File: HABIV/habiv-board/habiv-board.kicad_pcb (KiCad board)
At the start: 4 copper layers, 113 parts, among them IC1 RTC_PCF8523T, J10 Conn_01x08_Male, J2 Conn_ARM_JTAG_SWD_20, J3 Conn_01x02_Male, J4 Conn_01x16_Male, J5 Conn_01x02_Male, J6 Conn_01x16_Male, J7 Conn_01x16_Male, J8 Conn_01x08_Male, J9 Conn_01x02_Male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

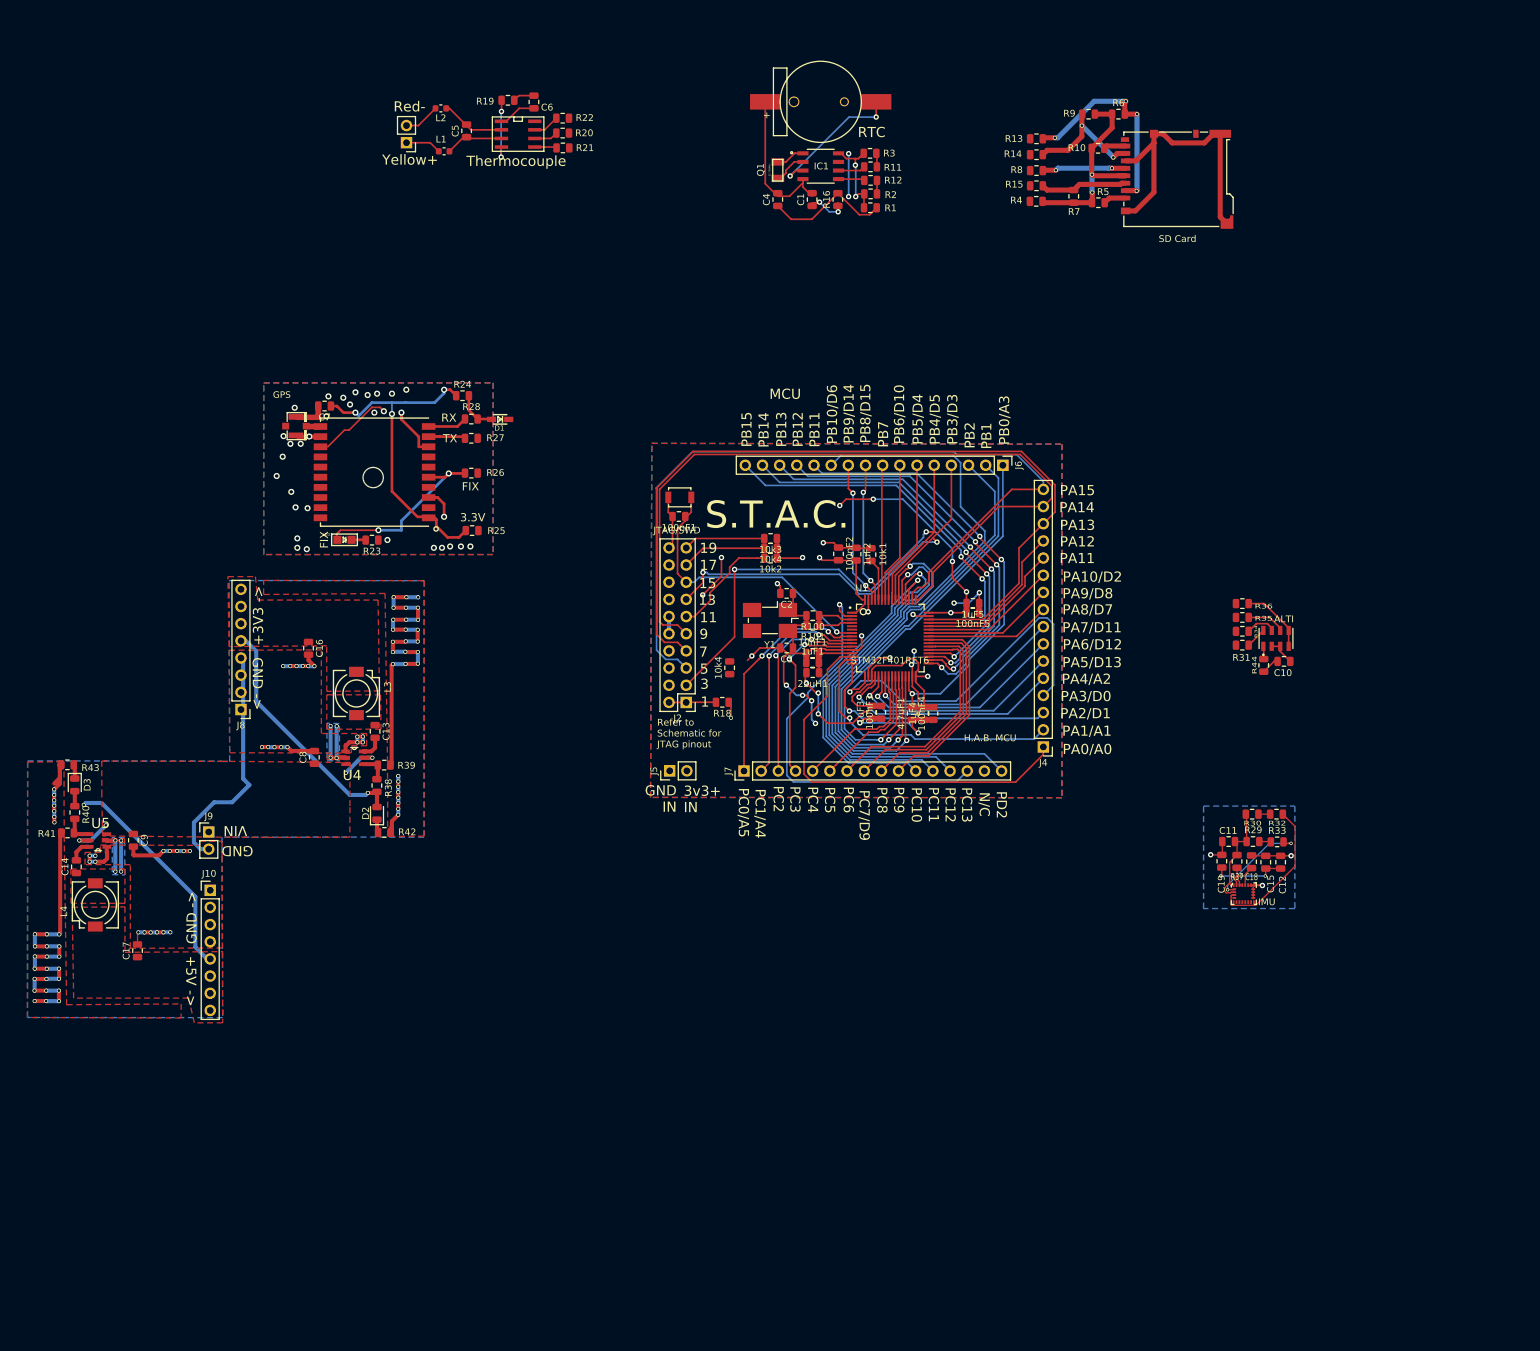
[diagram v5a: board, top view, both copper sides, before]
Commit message: begin to route together final nets
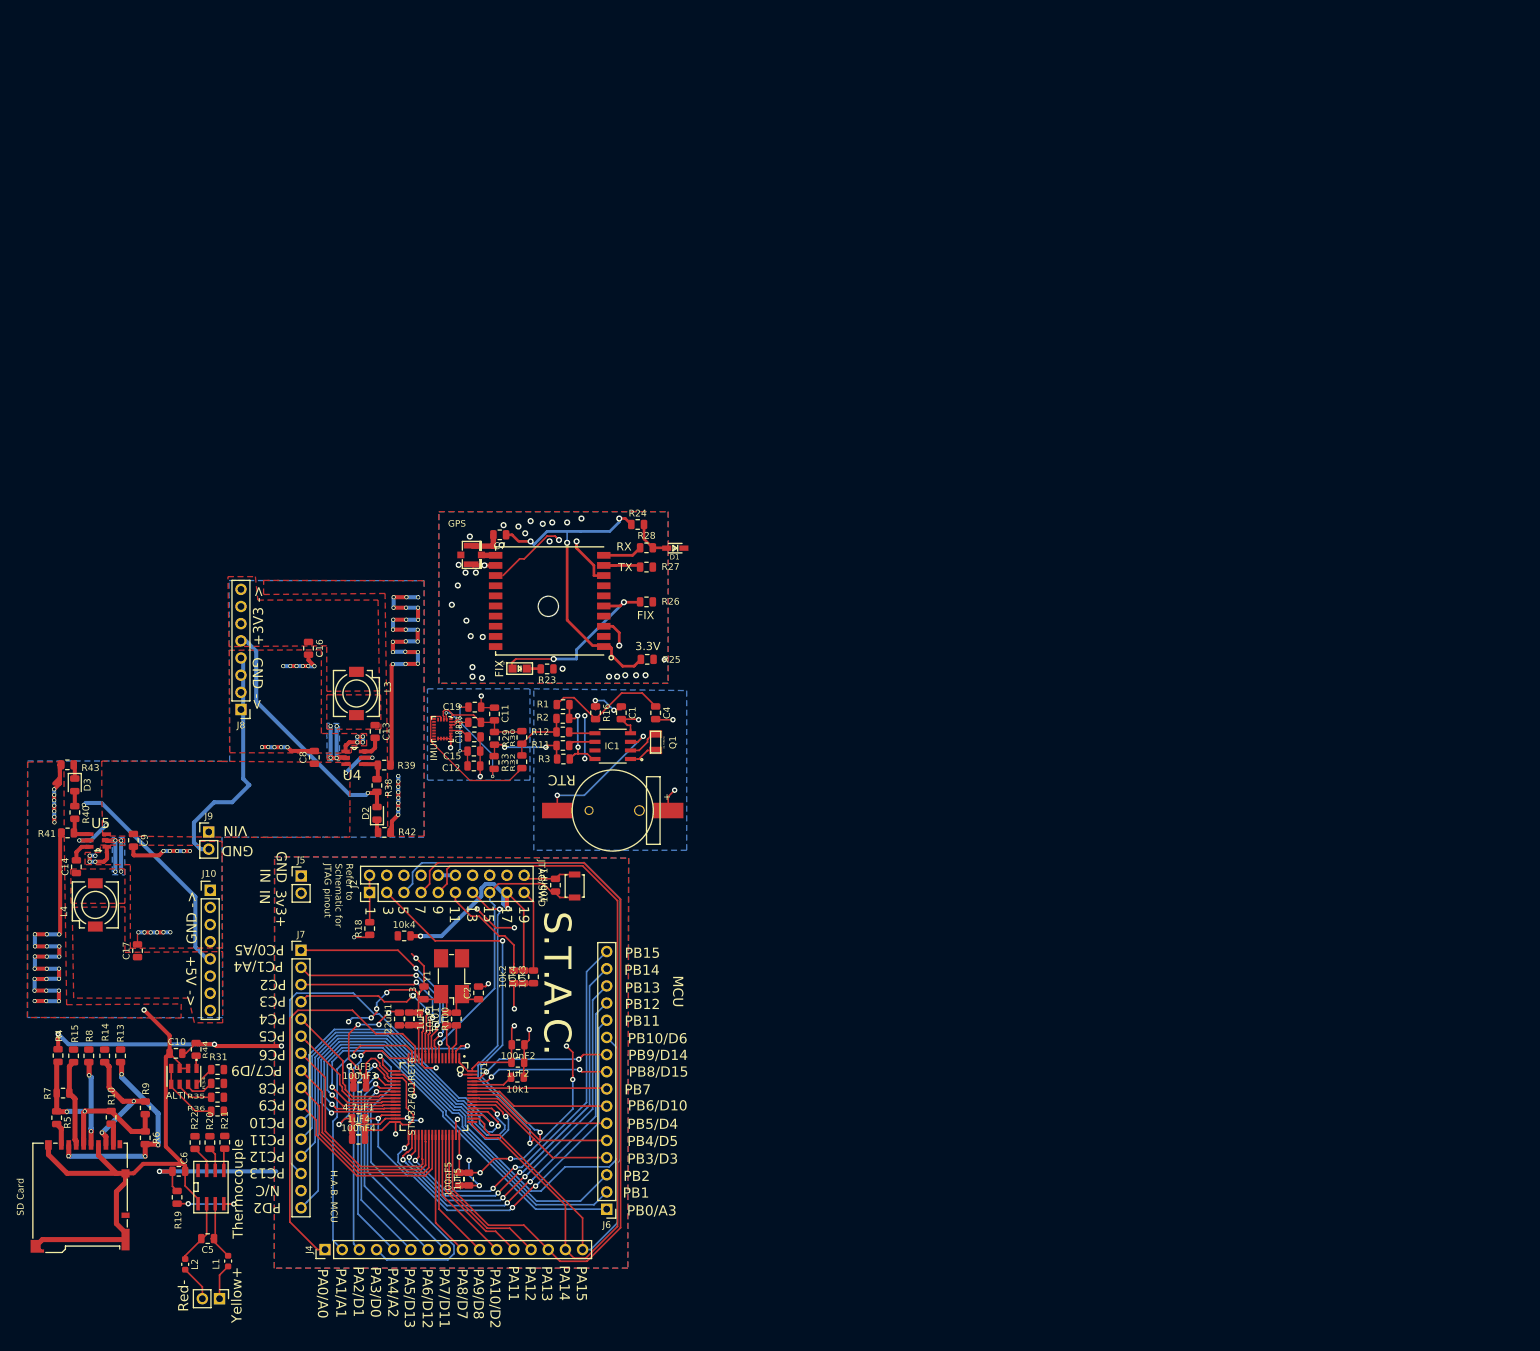
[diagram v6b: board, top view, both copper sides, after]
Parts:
- moved SD Card 221.3 mm to (24.1, 183.8), turned to 0 degrees
- moved R6 208.9 mm to (33.7, 175.1), turned to 270 degrees
- moved R5 205.1 mm to (20.6, 172.1), turned to 270 degrees
- moved R10 204.6 mm to (28.7, 172.1), turned to 270 degrees
- moved R9 202.7 mm to (33.7, 170.7), turned to 90 degrees
- moved R7 199.9 mm to (21.5, 168.5), turned to 180 degrees
- moved R4 192.1 mm to (20.8, 163.0), turned to 270 degrees
- moved R15 192.0 mm to (23.1, 163.0), turned to 270 degrees
- moved R8 191.8 mm to (25.4, 163.0), turned to 90 degrees
- moved R14 191.7 mm to (27.7, 163.0), turned to 90 degrees
- moved R13 191.7 mm to (30.1, 163.0), turned to 270 degrees
- moved L2 175.1 mm to (39.6, 193.8), turned to 270 degrees
- moved U7 174.1 mm to (39.4, 166.0), turned to 270 degrees
- moved C10 173.8 mm to (38.2, 162.6), turned to 180 degrees
- moved J3 173.2 mm to (44.7, 198.9), turned to 270 degrees
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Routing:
- net +3V3: track 158.2 -> 216.2 mm, vias 12 -> 17
- net GND: track 425.8 -> 450.8 mm, vias 139 -> 143
- net Net-(10k4-Pad2): track 12.4 -> 35.6 mm, vias 0 -> 2
- net PB8: track 24.5 -> 34.0 mm, vias 2 -> 4
- net PB9: track 25.1 -> 30.9 mm
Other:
- net class Default: trace_width 0.2 -> 0.6; via_dia 0.5 -> 0.8; via_drill 0.3 -> 0.4

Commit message: finish most of connections for 4 layer
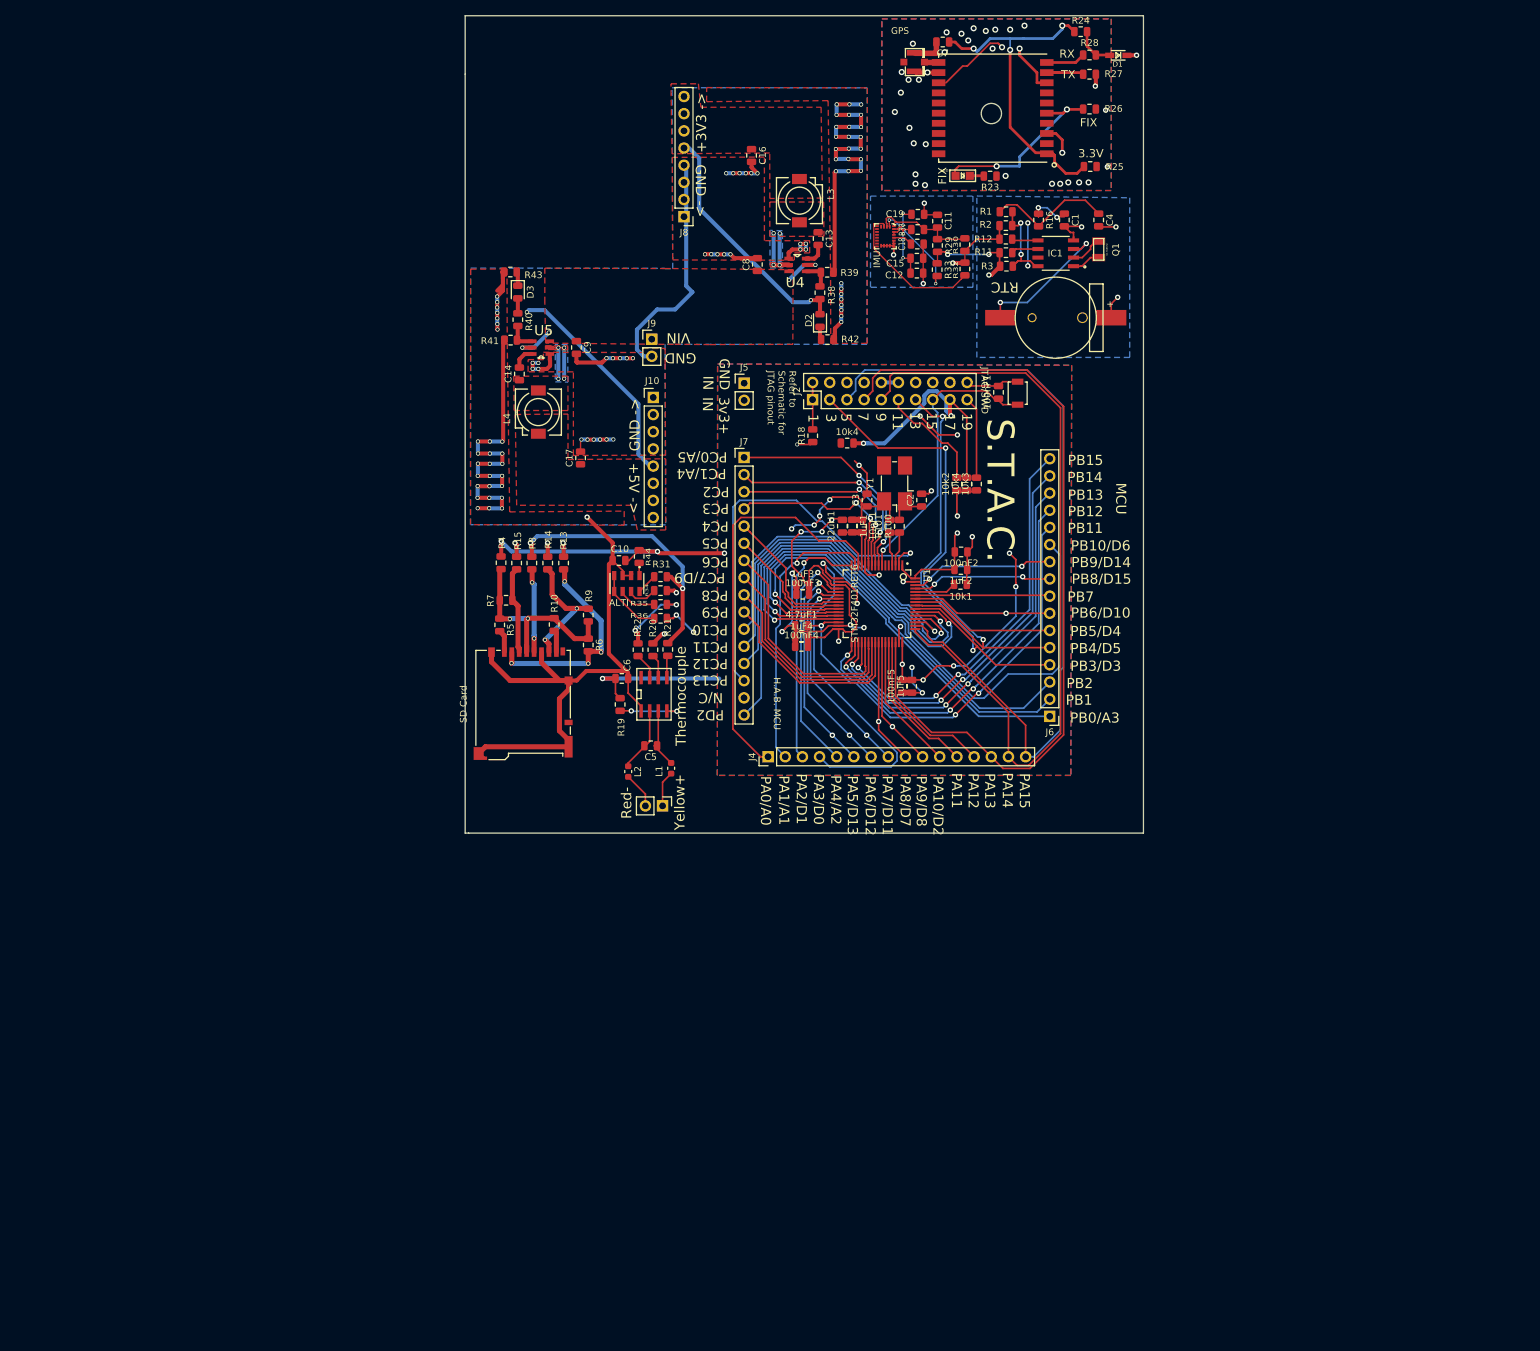
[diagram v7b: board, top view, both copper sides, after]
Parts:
- moved 100nF3 98.0 mm to (131.0, 94.7)
- moved 10k1 98.0 mm to (154.3, 93.3)
- moved 10k4 98.0 mm to (137.5, 72.4)
- moved 1uF3 98.0 mm to (131.0, 93.4)
- moved 1uF4 98.0 mm to (130.8, 101.1)
- moved 4.7uF1 98.0 mm to (130.8, 99.4)
- moved C17 98.0 mm to (98.1, 74.6)
- moved C2 98.0 mm to (148.5, 80.8)
- moved C3 98.0 mm to (140.5, 80.8)
- moved C5 98.0 mm to (108.5, 117.1)
- moved J7 98.0 mm to (122.3, 74.5)
- moved L2 98.0 mm to (105.1, 120.9)
- moved R21 98.0 mm to (111.0, 102.9)
- moved R34 98.0 mm to (109.9, 94.2)
- moved R36 98.0 mm to (109.9, 98.3)
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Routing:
- net PA10: track 20.3 -> 136.9 mm, vias 0 -> 1
- net PA5: track 33.0 -> 138.2 mm, vias 1 -> 4
- net PA7: track 31.5 -> 134.9 mm, vias 1 -> 4
- net PB6: track 20.8 -> 110.1 mm, vias 0 -> 2
- net PA6: track 32.3 -> 102.0 mm, vias 1 -> 5
- net PA9: track 19.4 -> 81.5 mm, vias 0 -> 2
- net PB15: track 60.2 -> 115.2 mm, vias 3 -> 4
- net PB8: track 34.0 -> 86.1 mm, vias 4 -> 5
- net PB9: track 30.9 -> 81.8 mm, vias 2 -> 3
- net PA8: track 18.6 -> 58.2 mm, vias 0 -> 3
- net PC7: track 32.8 -> 50.3 mm, vias 0 -> 1
- net GND: vias 143 -> 144
- net +3V3: vias 17 -> 16
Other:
- board outline added: 100.3 x 120.9 mm
- net class Default: clearance 0.1 -> 0.2
- rule trace_clearance: 0.1 -> 0.2

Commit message: finalize rough draft board
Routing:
- net +3V3: track 216.2 -> 272.6 mm, vias 16 -> 18
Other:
- outline, holes or cut-outs redrawn
- net class Default: trace_width 0.6 -> 0.25
